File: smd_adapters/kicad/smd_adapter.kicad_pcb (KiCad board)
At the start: 2 copper layers, 105 x 71.2 mm, 28 parts

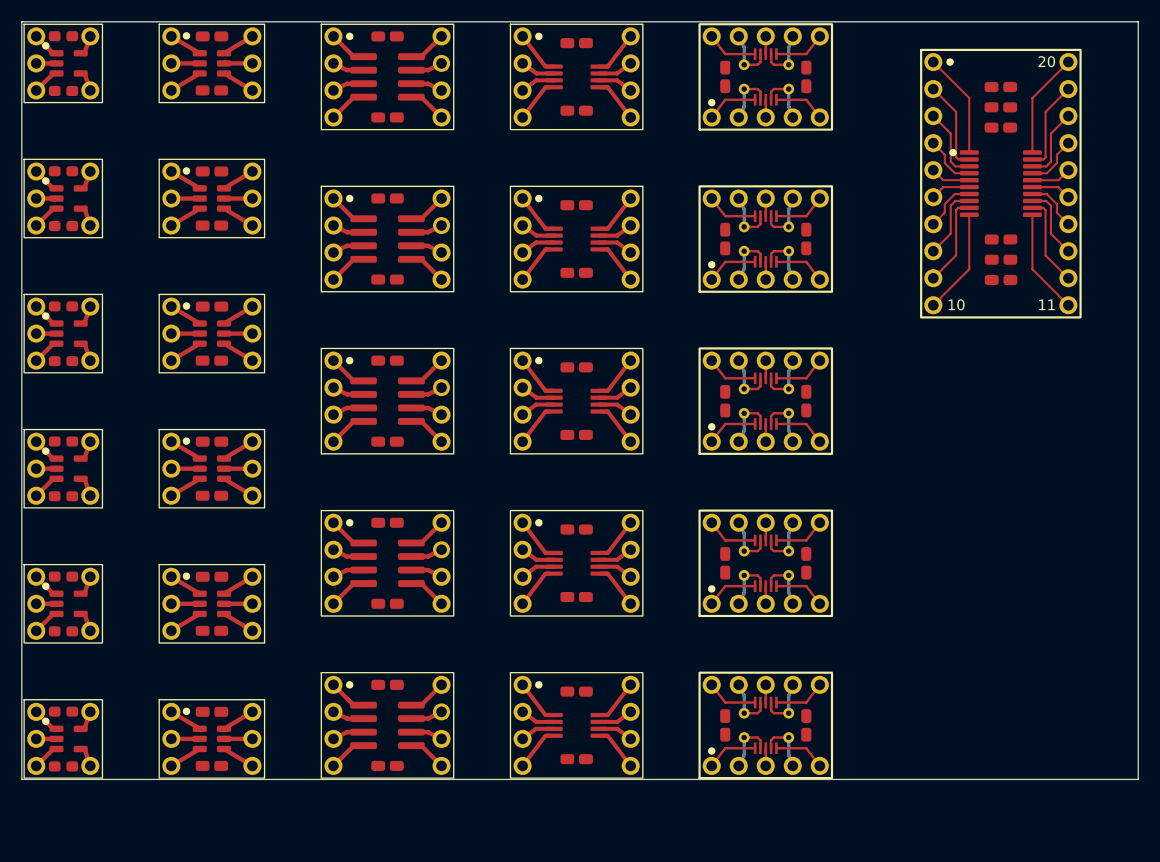
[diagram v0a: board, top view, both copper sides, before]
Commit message: Cleaned up the GreenPAK TSSOP-20 smd adapter
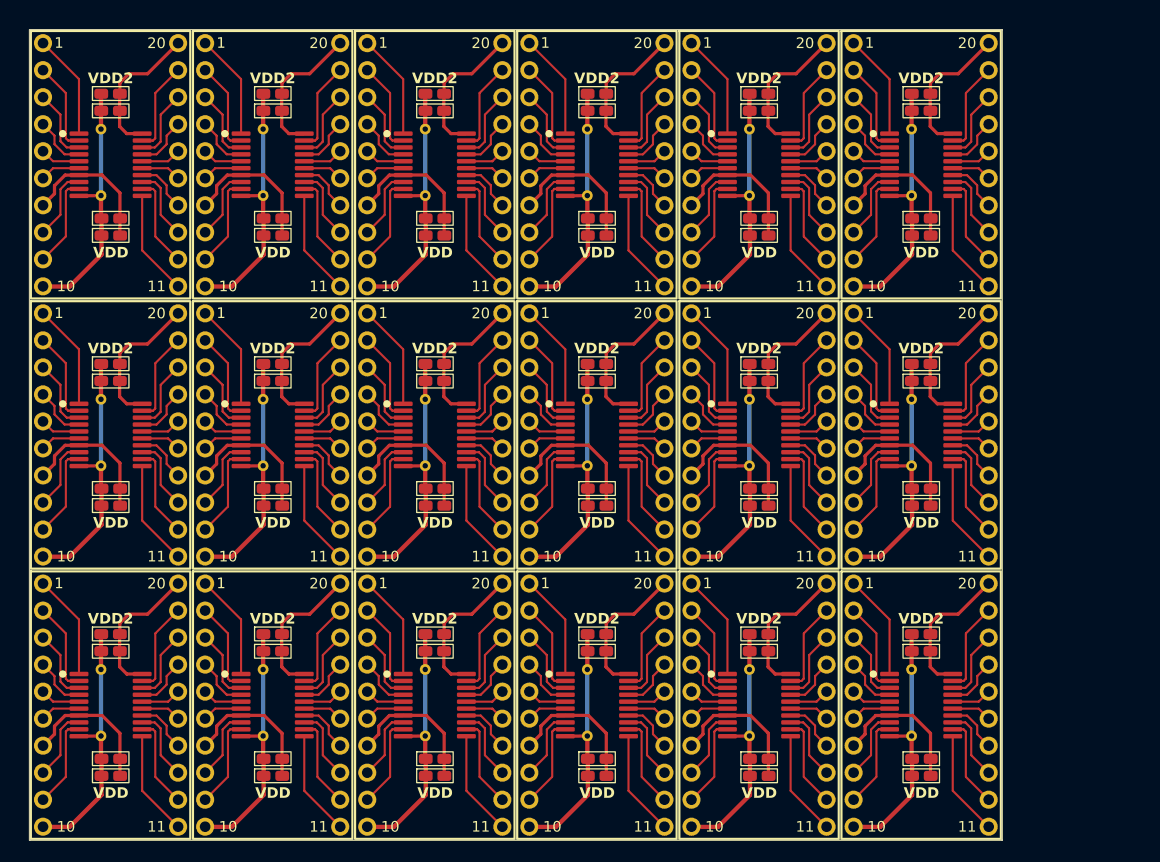
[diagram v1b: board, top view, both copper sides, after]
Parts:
- removed the REF** at (76.8, 40.6)
- removed the REF** at (90.2, 66.0)
- removed the REF** at (90.2, 40.6)
- removed the REF** at (142.2, 59.7)
- removed the REF** at (142.2, 90.2)
- removed the REF** at (106.7, 90.2)
- removed the REF** at (106.7, 74.9)
- removed the REF** at (76.8, 27.9)
- removed the REF** at (124.5, 59.7)
- removed the REF** at (90.2, 78.7)
- removed the REF** at (142.2, 74.9)
- removed the REF** at (124.5, 29.2)
- removed the REF** at (124.5, 44.5)
- removed the REF** at (76.8, 66.0)
- removed the REF** at (76.8, 91.4)
- removed the REF** at (90.2, 91.4)
- removed the REF** at (142.2, 29.2)
- removed the REF** at (76.8, 78.7)
- removed the REF** at (124.5, 90.2)
- removed the REF** at (90.2, 53.3)
- removed the REF** at (106.7, 29.2)
- removed the REF** at (142.2, 44.5)
- removed the REF** at (124.5, 74.9)
- removed the REF** at (90.2, 27.9)
- removed the REF** at (76.8, 53.3)
- removed the REF** at (106.7, 44.5)
- removed the REF** at (106.7, 59.7)
- added REF**: GREENPAK-SMD-ADAPTER-TSSOP-20, smd_adapter:GREENPAK-SMD-ADAPTER-TSSOP-20, F.Cu at (156.8, 62.9)
- added REF**: GREENPAK-SMD-ADAPTER-TSSOP-20, smd_adapter:GREENPAK-SMD-ADAPTER-TSSOP-20, F.Cu at (111.1, 37.5)
- added REF**: GREENPAK-SMD-ADAPTER-TSSOP-20, smd_adapter:GREENPAK-SMD-ADAPTER-TSSOP-20, F.Cu at (80.6, 88.3)
- added REF**: GREENPAK-SMD-ADAPTER-TSSOP-20, smd_adapter:GREENPAK-SMD-ADAPTER-TSSOP-20, F.Cu at (95.9, 88.3)
- added REF**: GREENPAK-SMD-ADAPTER-TSSOP-20, smd_adapter:GREENPAK-SMD-ADAPTER-TSSOP-20, F.Cu at (156.8, 37.5)
- added REF**: GREENPAK-SMD-ADAPTER-TSSOP-20, smd_adapter:GREENPAK-SMD-ADAPTER-TSSOP-20, F.Cu at (156.8, 88.3)
- added REF**: GREENPAK-SMD-ADAPTER-TSSOP-20, smd_adapter:GREENPAK-SMD-ADAPTER-TSSOP-20, F.Cu at (95.9, 62.9)
- added REF**: GREENPAK-SMD-ADAPTER-TSSOP-20, smd_adapter:GREENPAK-SMD-ADAPTER-TSSOP-20, F.Cu at (80.6, 62.9)
- added REF**: GREENPAK-SMD-ADAPTER-TSSOP-20, smd_adapter:GREENPAK-SMD-ADAPTER-TSSOP-20, F.Cu at (141.6, 88.3)
- added REF**: GREENPAK-SMD-ADAPTER-TSSOP-20, smd_adapter:GREENPAK-SMD-ADAPTER-TSSOP-20, F.Cu at (126.4, 62.9)
- added REF**: GREENPAK-SMD-ADAPTER-TSSOP-20, smd_adapter:GREENPAK-SMD-ADAPTER-TSSOP-20, F.Cu at (111.1, 88.3)
- added REF**: GREENPAK-SMD-ADAPTER-TSSOP-20, smd_adapter:GREENPAK-SMD-ADAPTER-TSSOP-20, F.Cu at (141.6, 37.5)
- added REF**: GREENPAK-SMD-ADAPTER-TSSOP-20, smd_adapter:GREENPAK-SMD-ADAPTER-TSSOP-20, F.Cu at (126.4, 88.3)
- added REF**: GREENPAK-SMD-ADAPTER-TSSOP-20, smd_adapter:GREENPAK-SMD-ADAPTER-TSSOP-20, F.Cu at (141.6, 62.9)
- added REF**: GREENPAK-SMD-ADAPTER-TSSOP-20, smd_adapter:GREENPAK-SMD-ADAPTER-TSSOP-20, F.Cu at (126.4, 37.5)
- added REF**: GREENPAK-SMD-ADAPTER-TSSOP-20, smd_adapter:GREENPAK-SMD-ADAPTER-TSSOP-20, F.Cu at (111.1, 62.9)
- added REF**: GREENPAK-SMD-ADAPTER-TSSOP-20, smd_adapter:GREENPAK-SMD-ADAPTER-TSSOP-20, F.Cu at (95.9, 37.5)
- REF**: value SMD_ADAPTER_TSSOP-20 -> GREENPAK-SMD-ADAPTER-TSSOP-20; footprint smd_adapter:SMD_ADAPTER_TSSOP-20 -> smd_adapter:GREENPAK-SMD-ADAPTER-TSSOP-20
- moved REF** 83.7 mm to (80.6, 37.5)
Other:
- board size 105 x 71.2 mm -> 91.4 x 76.2 mm
